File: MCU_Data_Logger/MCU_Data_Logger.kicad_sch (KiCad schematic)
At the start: 0 parts

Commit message: Set up the SHC of the project
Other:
- title: (none) -> ${Project_Name}
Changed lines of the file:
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@@
 	(generator_version "9.0")
 	(paper "A4")
+	(title_block
+		(title "${Project_Name}")
+		(date "2025-12-27")
+		(rev "V1")
+	)
 	(sheet_instances
 		(path "/"

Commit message: Add connector sheet file and put the syumpols on the sch for both main sheet and connector sheet and assigne the footprint to each sympol
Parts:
- added BT1: Battery, Connector_PinHeader_2.54mm:PinHeader_1x02_P2.54mm_Vertical, symbol Device:Battery
- added C1, C2: 22pF, Capacitor_SMD:C_0805_2012Metric, symbol Device:C
- added C3, C4: 0.1uF, Capacitor_SMD:C_0805_2012Metric, symbol Device:C
- added C5: 100nF, Capacitor_SMD:C_0805_2012Metric, symbol Device:C_Polarized
- added D1, D2: LED, LED_SMD:LED_0805_2012Metric, symbol Device:LED
- added H1, H2, H3, H4: MountingHole, MountingHole:MountingHole_2.1mm, symbol Mechanical:MountingHole
- added R1, R2, R7: 10K, Resistor_SMD:R_0805_2012Metric, symbol Device:R
- added R3, R4: 330, Resistor_SMD:R_0805_2012Metric, symbol Device:R
- added R5, R6: 4.7K, Resistor_SMD:R_0805_2012Metric, symbol Device:R
- added U1, U2: 24LC1025, Package_SO:SOIC-8_3.9x4.9mm_P1.27mm, symbol Memory_EEPROM:24LC1025
- added U3: DS1337S_, Footprints:SOIC127P600X175-8N, symbol DS1337S_:DS1337S_
- added U4: ATMEGA328P-AU, Footprints:QFP80P900X900X120-32N, symbol ATMEGA328P-AU:ATMEGA328P-AU
- added Y1: 16MHz, Crystal:Crystal_SMD_5032-2Pin_5.0x3.2mm, symbol Device:Crystal
- added Y2: 32.768KHz, Crystal:Crystal_SMD_5032-2Pin_5.0x3.2mm, symbol Device:Crystal
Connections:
- new net GND: U4.21 (GND), U4.3 (GND), U4.5 (GND)
- new net VCC: U4.4 (VCC), U4.6 (VCC)
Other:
- added sheet Connectors (Connectors.kicad_sch)

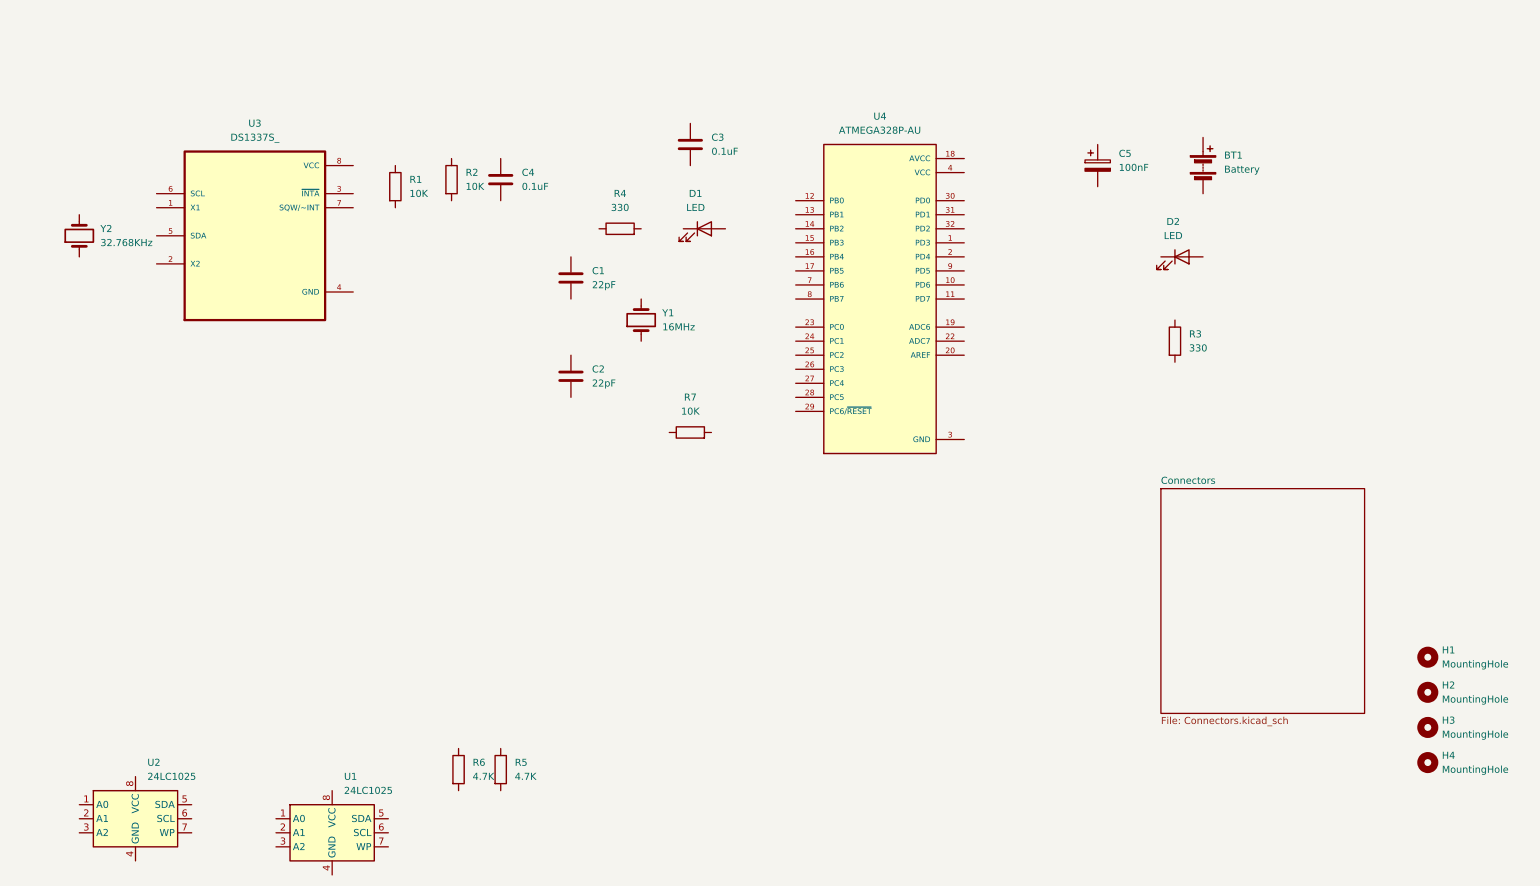
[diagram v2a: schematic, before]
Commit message: finlize sch wiring
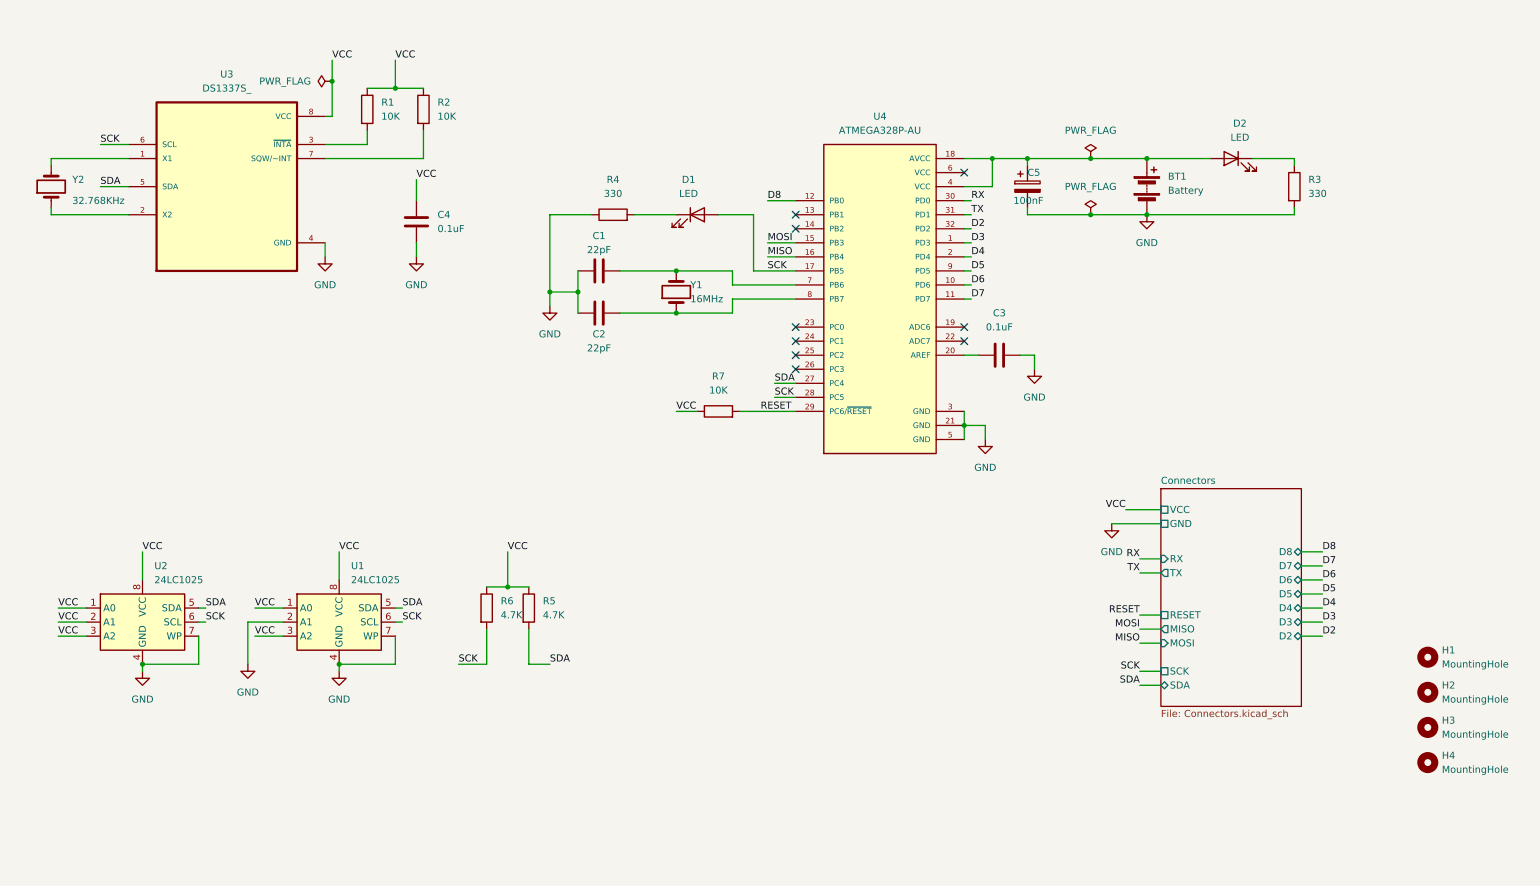
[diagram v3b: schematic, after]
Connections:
- net GND: now also BT1.2 (-), C1.1, C2.1, C3.2, C4.2, C5.2, R3.2, R4.1, U1.2 (A1), U1.4 (GND), U1.7 (WP), U2.4 (GND), U2.7 (WP), U3.4 (GND)
- net VCC: now also C4.1, R1.1, R2.1, R5.1, R6.1, R7.1, U1.1 (A0), U1.3 (A2), U1.8 (VCC), U2.1 (A0), U2.2 (A1), U2.3 (A2), U2.8 (VCC), U3.8 (VCC); no longer U4.4 (VCC), U4.6 (VCC)
- net at D1.1 (K): now also R4.2
- net SCK: now reaches D1.2 (A)
- net SCK: now also R6.2, U1.6 (SCL), U2.6 (SCL), U3.6 (SCL), U4.17 (PB5), U4.28 (PC5)
- net at R3.1: now also D2.1 (K)
- net at C5.1: now also BT1.1 (+), D2.2 (A), U4.18 (AVCC), U4.4 (VCC)
- net at R2.2: now also U3.7 (SQW/~INT)
- net at R1.2: now also U3.3 (~{INTA})
- net at Y2.1: now also U3.2 (X2)
- net at Y2.2: now also U3.1 (X1)
- net at Y1.1: now also C2.2, U4.8 (PB7)
- net at Y1.2: now also C1.2, U4.7 (PB6)
- net D3: now reaches U4.1 (PD3)
- net D6: now reaches U4.10 (PD6)
- net D7: now reaches U4.11 (PD7)
- net D8: now reaches U4.12 (PB0)
- net MOSI: now reaches U4.15 (PB3)
- net MISO: now reaches U4.16 (PB4)
- net D4: now reaches U4.2 (PD4)
- net at U4.20 (AREF): now also C3.1
- net SDA: now reaches U4.27 (PC4)
- net SDA: now also R5.2, U1.5 (SDA), U2.5 (SDA), U3.5 (SDA)
- net RESET: now reaches U4.29 (PC6/~{RESET})
- net RESET: now also R7.2
- net RX: now reaches U4.30 (PD0)
- net TX: now reaches U4.31 (PD1)
- net D2: now reaches U4.32 (PD2)
- net D5: now reaches U4.9 (PD5)
- no-connect marks 0 -> 9
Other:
- sheet Connectors ports: added D2, D3, D4, D5, D6, D7, D8, GND, MISO, MOSI, RESET, RX, SCK, SDA, TX, VCC; removed none
- moved on the sheet: BT1, C1, C2, C3, C4, C5, D1, D2, R1, R2, R3, R4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

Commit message: Add the layout of the board and finlize the first version of datalogger board
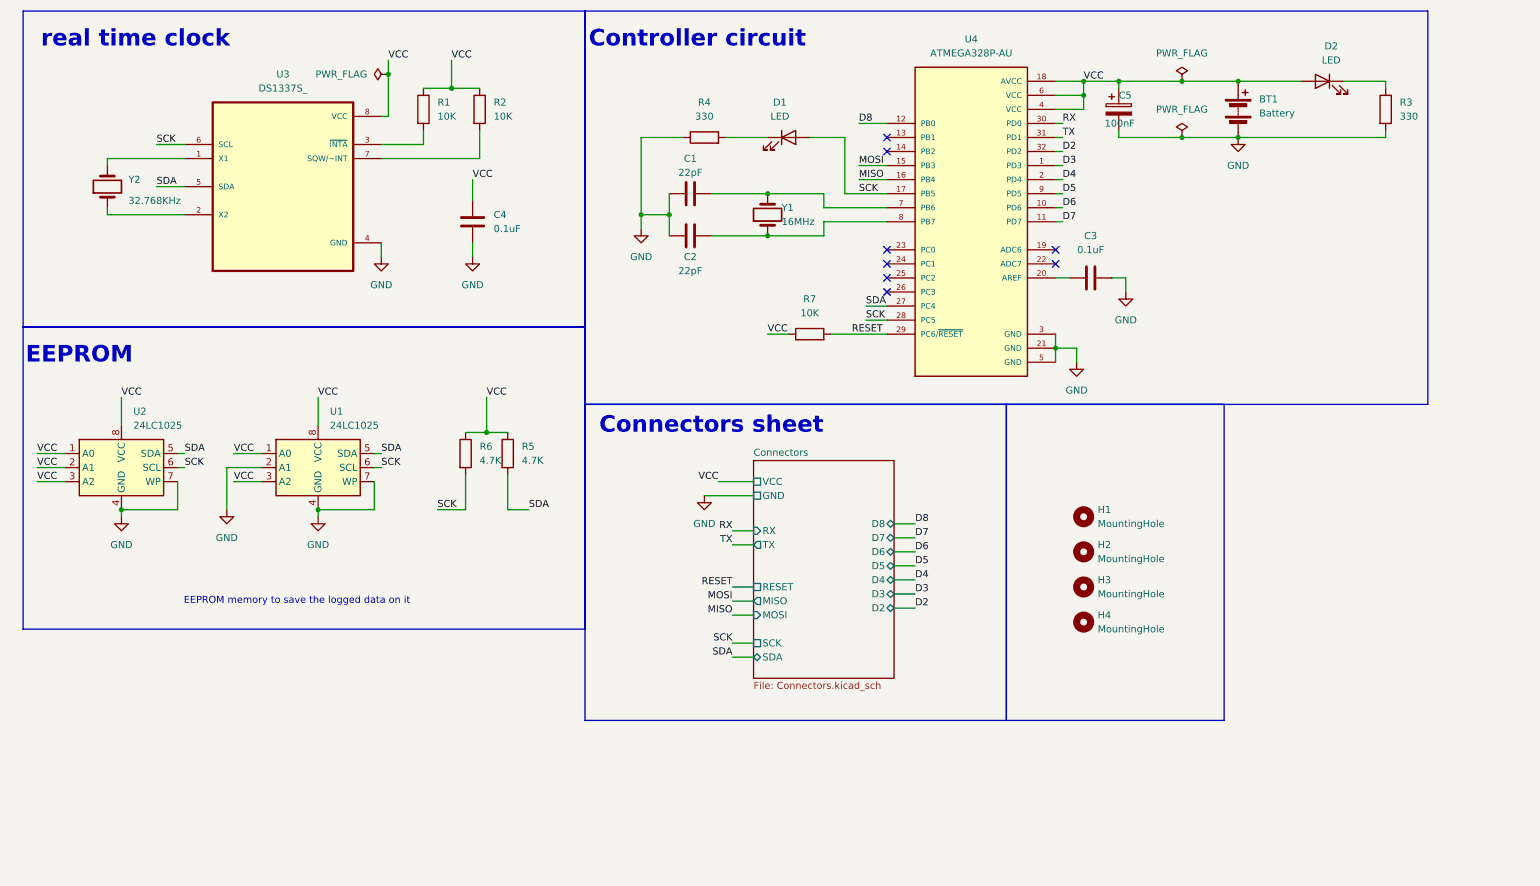
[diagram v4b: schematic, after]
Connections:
- net VCC: now also BT1.1 (+), C5.1, D2.2 (A), U4.18 (AVCC), U4.4 (VCC), U4.6 (VCC)
- no-connect marks 9 -> 8
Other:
- note added: "Connectors sheet"
- note added: "Controller circuit"
- note added: "EEPROM"
- note added: "EEPROM memory to save the logged data on it"
- note added: "real time clock"
- moved on the sheet: BT1, C1, C2, C3, C4, C5, D1, D2, H1, H2, H3, H4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
